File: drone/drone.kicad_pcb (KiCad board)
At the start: 2 copper layers, 50.8 x 50.8 mm, 40 parts, among them J1 Conn_01x06, J2 Conn_01x02, J3 Conn_01x02, J4 Conn_01x02, J5 Conn_01x02, J6 Conn_01x02, Q1 Si2319CDS, Q2 Si2319CDS, Q3 Si2319CDS, Q4 Si2319CDS, U1 ESP32-WROOM-32, U2 MPU-6050, U3 DWM1000, U4 BMP280, U5 TPS63001

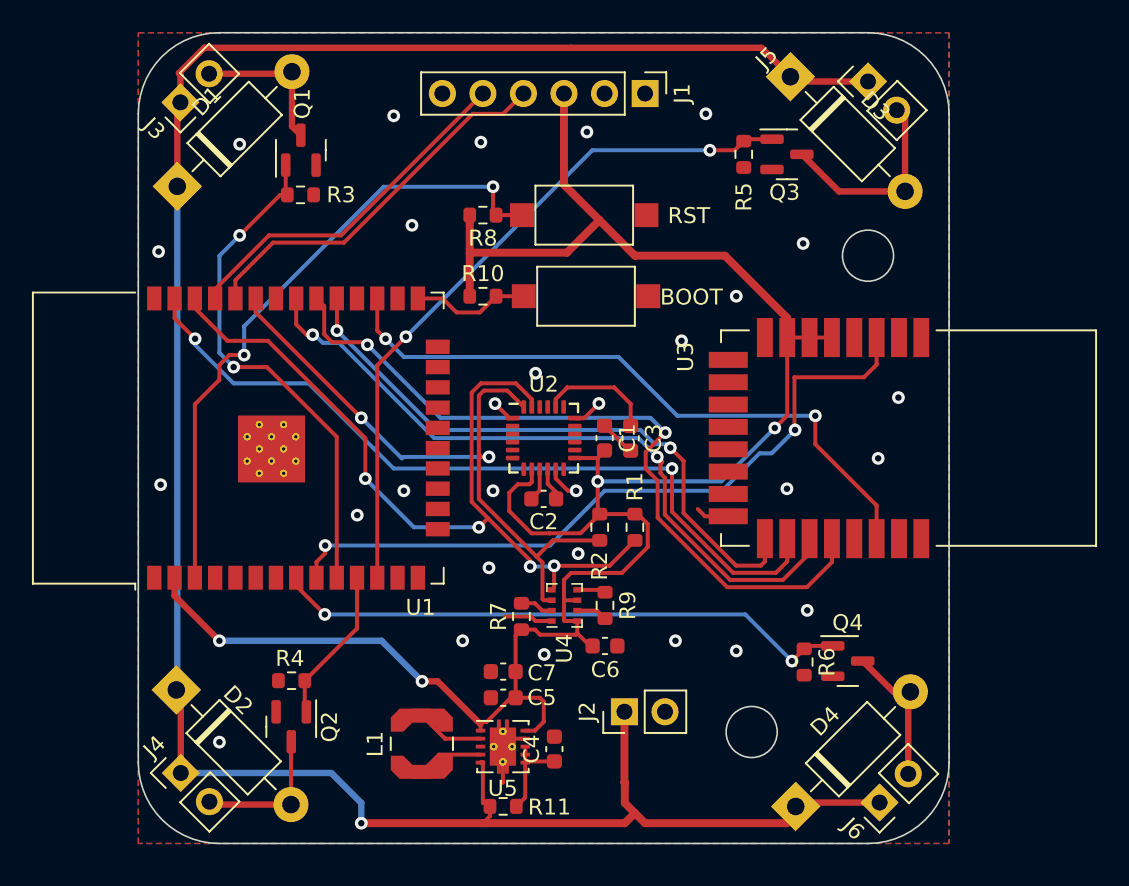
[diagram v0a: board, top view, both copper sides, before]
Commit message: add ws2812b + wiring
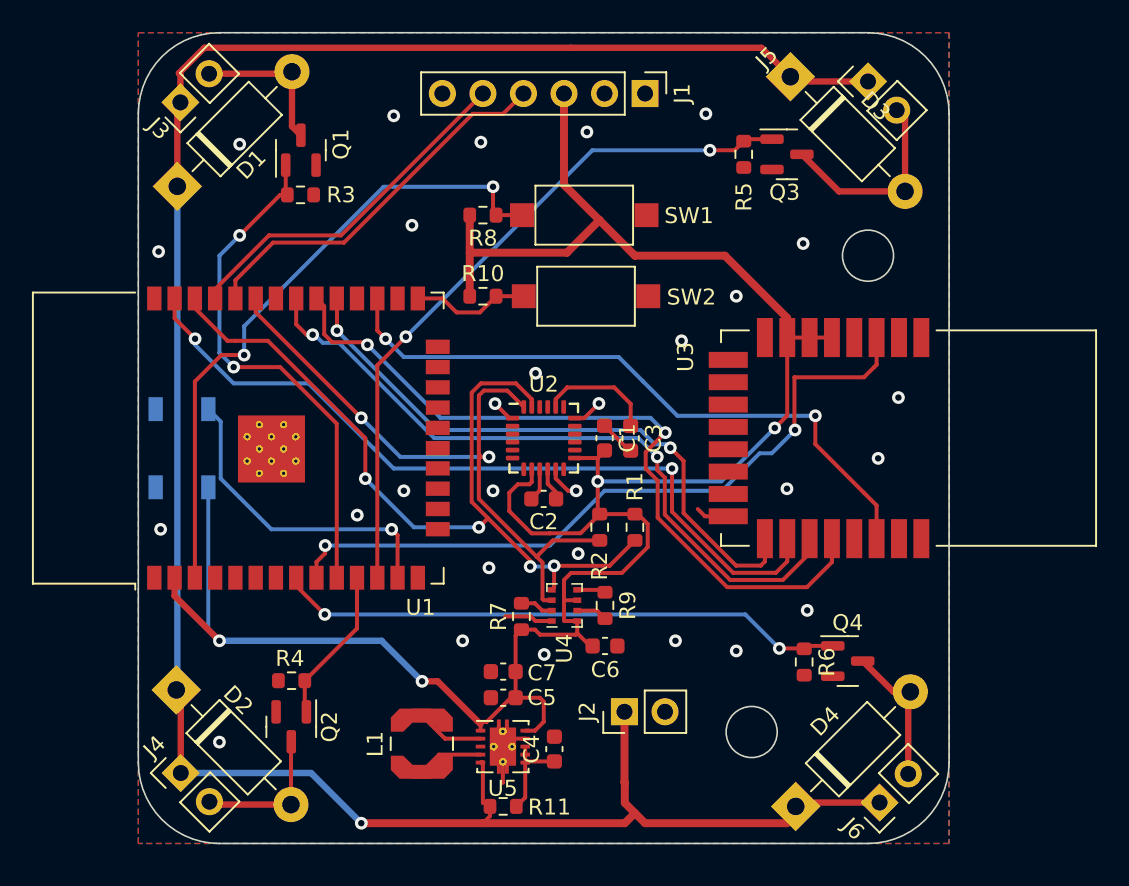
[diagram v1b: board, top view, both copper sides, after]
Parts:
- added D5: WS2812B, LED_SMD:LED_WS2812B_PLCC4_5.0x5.0mm_P3.2mm, B.Cu at (78.9, 102.2)
- renumbered RST to SW1, BOOT to SW2
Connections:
- U1 pad 13: unconnected-(U1-Pad13) -> Net-(U1-Pad13)
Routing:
- net Net-(U1-Pad13): track 0.00 -> 19.9 mm, vias 0 -> 1
- net VCC: track 132.7 -> 142.6 mm
- net BAT+: track 147.1 -> 146.4 mm
- net MOTOR_4: track 36.5 -> 35.8 mm

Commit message: add bat level wiring
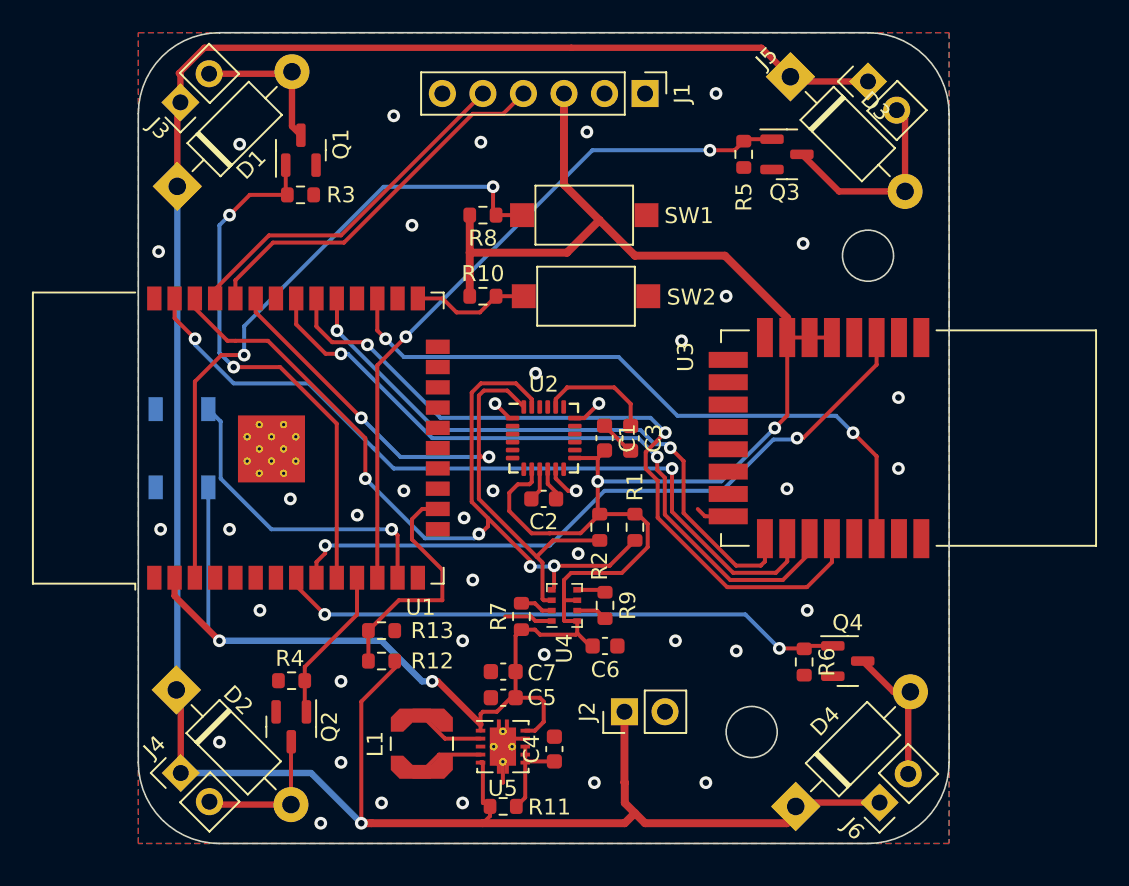
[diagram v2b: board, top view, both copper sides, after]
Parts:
- added R12: 100K, Resistor_SMD:R_0603_1608Metric, F.Cu at (91.4, 115.6)
- added R13: 100K, Resistor_SMD:R_0603_1608Metric, F.Cu at (91.4, 113.7)
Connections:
- U1 pad 16: unconnected-(U1-Pad16) -> BAT_LEVEL
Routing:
- net BAT_LEVEL: track 0.00 -> 15.1 mm
- net BAT+: track 146.4 -> 157.4 mm
- net DW_RST: track 45.2 -> 43.2 mm
- net MOTOR_1: track 32.7 -> 33.8 mm
- net SCL: track 52.6 -> 53.5 mm
- net DW_IRQ: track 41.0 -> 41.7 mm
- net GND: vias 29 -> 40
